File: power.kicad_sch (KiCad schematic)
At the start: 86 parts, among them Q10 2NPN, Q3 PMOS, Q4 PMOS, Q5 PMOS, Q6 PMOS, Q7 2NPN, Q9 2PNP, U21 TPS62410, U22 LDO-2V5, U28 AP22652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

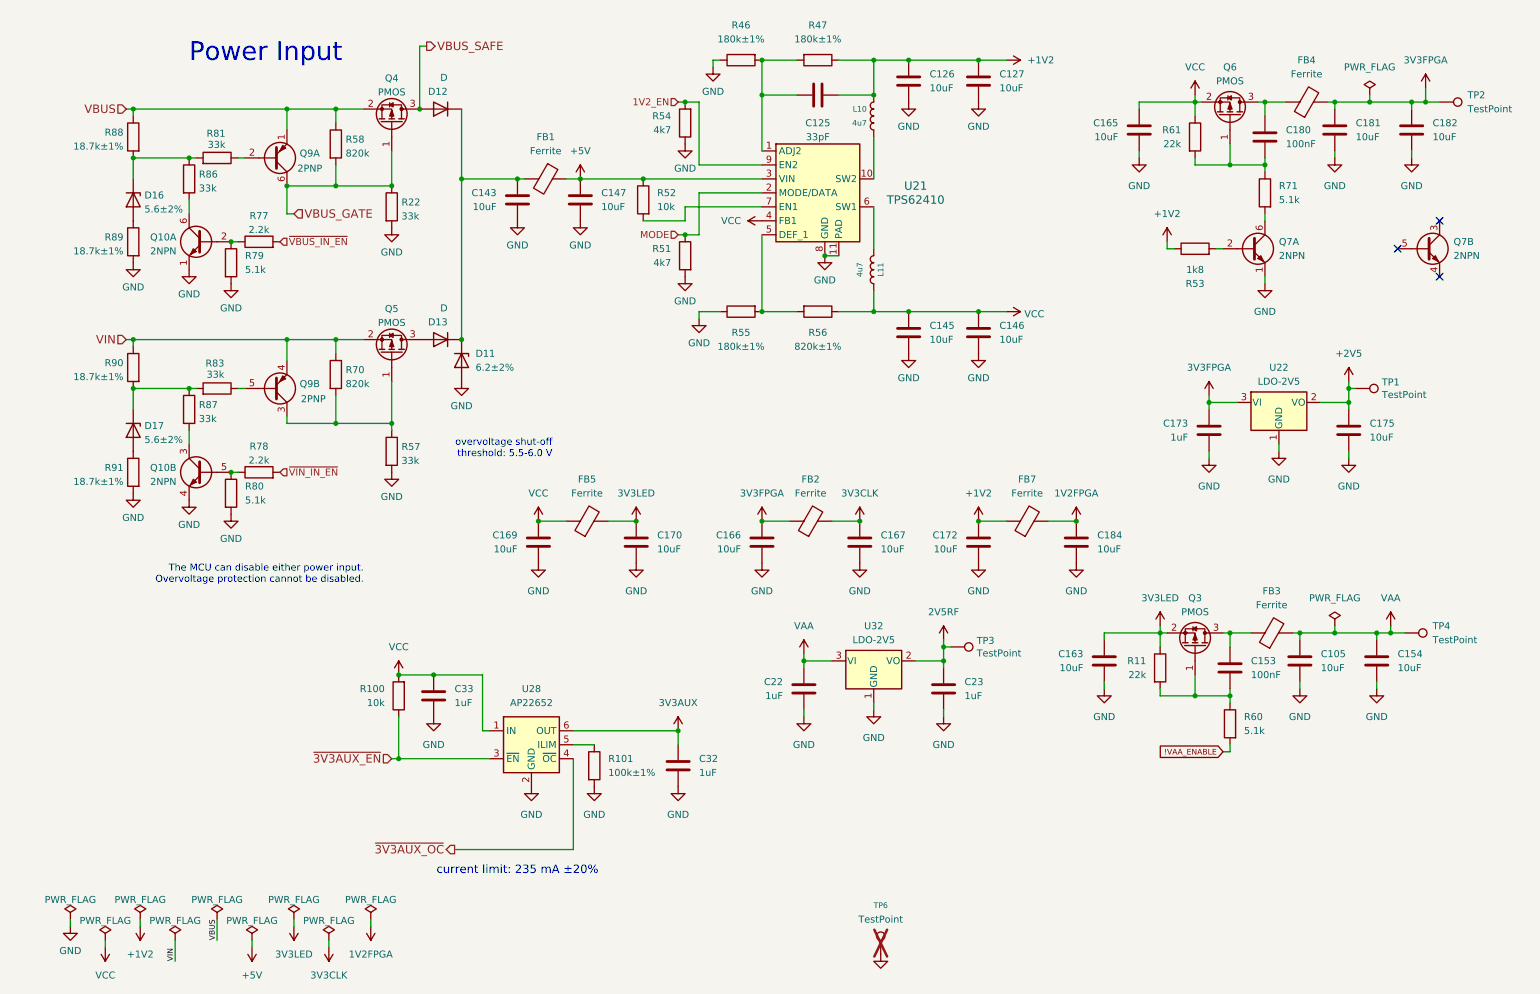
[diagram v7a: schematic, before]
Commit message: Add test points
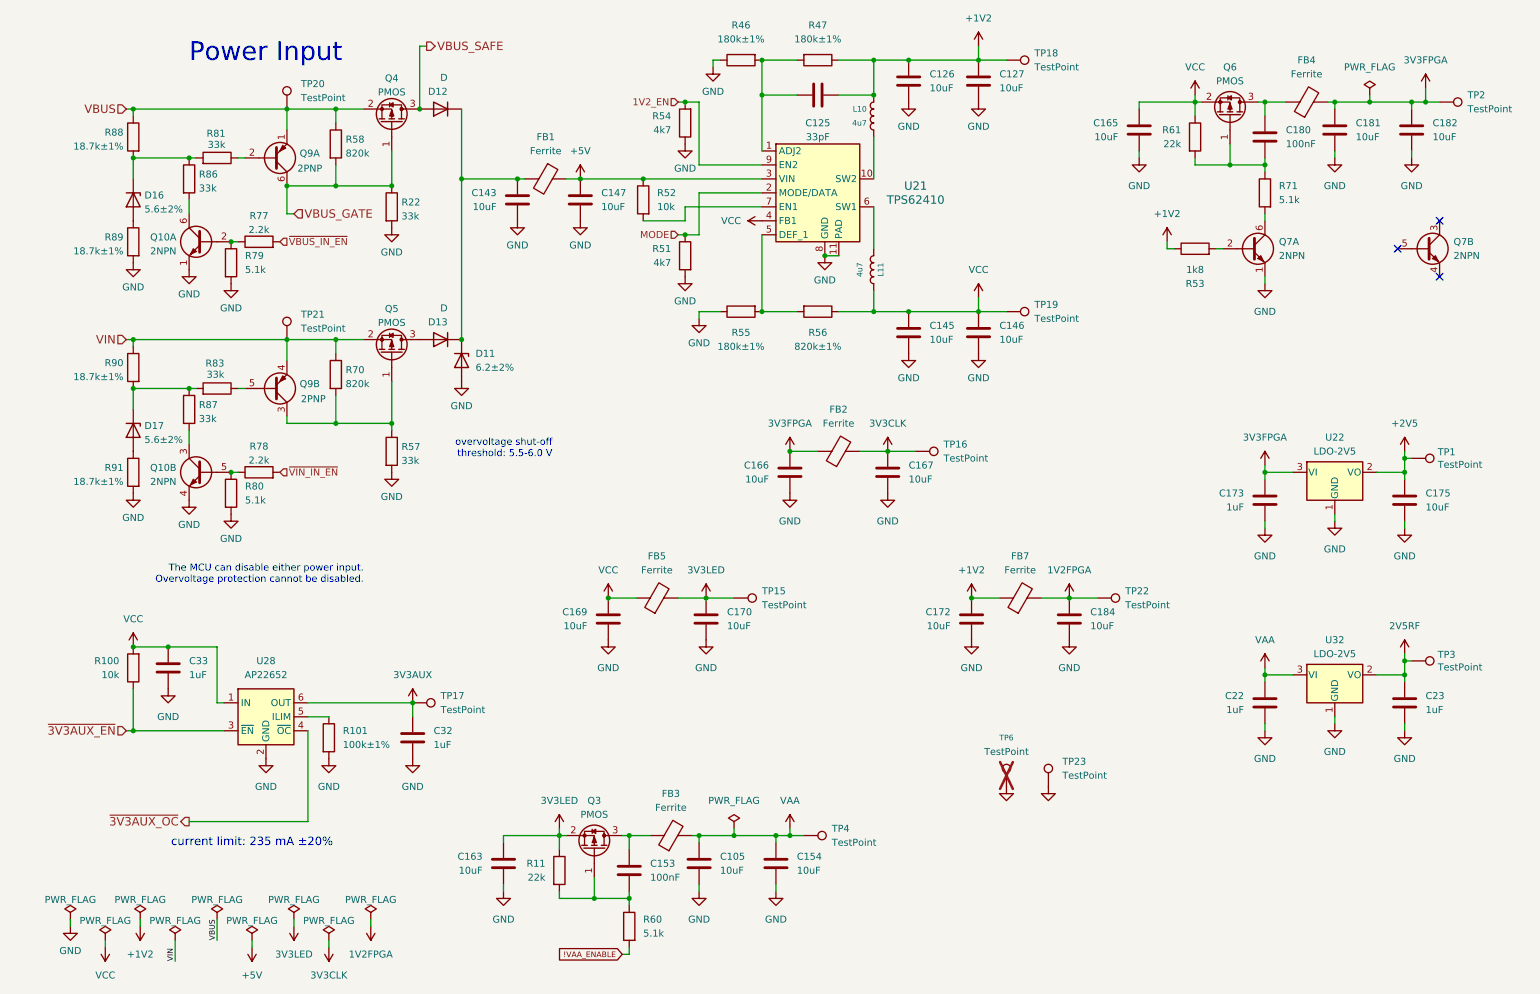
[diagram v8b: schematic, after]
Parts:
- added TP15, TP16, TP17, TP18, TP19, TP20, TP21, TP22, TP23: TestPoint, TestPoint:TestPoint_Pad_D1.0mm, symbol Connector:TestPoint
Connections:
- net +1V2: now also TP18.1
- net 1V2FPGA: now also TP22.1
- net 3V3AUX: now also TP17.1
- net 3V3CLK: now also TP16.1
- net 3V3LED: now also TP15.1
- net GND: now also TP23.1
- net VBUS: now also TP20.1
- net VCC: now also TP19.1
- net VIN: now also TP21.1
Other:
- moved on the sheet: C105, C153, C154, C163, C166, C167, C169, C170, C172, C173, C175, C184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
